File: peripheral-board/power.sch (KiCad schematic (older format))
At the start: 40 parts, among them CON4001 BARREL_JACK, Q4001 Q_PMOS_DGS, Q4002 Q_NMOS_DGS, U4001 AP1509, U4002 LM27313, U4003 LT3652

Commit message: power supply component placement
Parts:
- removed Q4001: Q_PMOS_DGS, symbol Q_PMOS_DGS
- removed Q4002: Q_NMOS_DGS, symbol Q_NMOS_DGS
- removed R4010, R4011: R, Resistors_SMD:R_0805, symbol R
- added Q4001: IRLML2244TRPbF, TO_SOT_Packages_SMD:SOT-23, symbol Q_PMOS_GSD
- C4007: value CP -> 100u
- C4010: value CP -> 220u
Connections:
- net labels added: SHDN_3, VAA, ~SHDN_24
- net labels removed: SHDN, VCC
- wire segments 82 -> 73
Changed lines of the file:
@@
 	1    0    0    -1
 $EndComp
-Text HLabel 950  3850 0    60   Input ~ 0
-SHDN
+Text HLabel 7300 5150 0    60   Input ~ 0
+SHDN_3
 $Comp
 L LT3652 U4003
@@
 BATTERY_NTC
 $Comp
-L PWR_FLAG #FLG4003
+L PWR_FLAG #FLG4004
 U 1 1 589AA4ED
 P 7500 2000
-F 0 "#FLG4003" H 7550 2050 50  0001 C CNN
+F 0 "#FLG4004" H 7550 2050 50  0001 C CNN
 F 1 "PWR_FLAG" H 7500 2174 50  0000 C CNN
 F 2 "" H -550 -1000 50  0001 C CNN
@@
 	0    -1   -1   0
 $EndComp
-$Comp
-L Q_PMOS_DGS Q4001
-U 1 1 589B3C76
-P 9750 1200
-F 0 "Q4001" V 10000 1200 50  0000 C CNN
-F 1 "Q_PMOS_DGS" V 10091 1200 50  0000 C CNN
-F 2 "" H 4850 -2550 50  0001 C CNN
-F 3 "" H 4650 -2650 50  0001 C CNN
-	1    9750 1200
-	0    -1   1    0
-$EndComp
 Connection ~ 10150 1300
 $Comp
@@
 	9950 1300 10950 1300
 $Comp
-L VCC #PWR4005
-U 1 1 589B6465
-P 10950 1300
-F 0 "#PWR4005" H 6250 -3050 50  0001 C CNN
-F 1 "VCC" H 10967 1473 50  0000 C CNN
-F 2 "" H 6250 -2900 50  0001 C CNN
-F 3 "" H 6250 -2900 50  0001 C CNN
-	1    10950 1300
-	1    0    0    -1
-$EndComp
-$Comp
 L PWR_FLAG #FLG4002
 U 1 1 589B64BF
@@
 P 9300 5400
 F 0 "C4010" H 9418 5446 50  0000 L CNN
-F 1 "CP" H 9418 5355 50  0000 L CNN
+F 1 "220u" H 9418 5355 50  0000 L CNN
 F 2 "" H 1088 -350 50  0001 C CNN
 F 3 "" H 1050 -200 50  0001 C CNN
@@
 P 7700 4600
 F 0 "C4007" V 7445 4600 50  0000 C CNN
-F 1 "CP" V 7536 4600 50  0000 C CNN
+F 1 "100u" V 7536 4600 50  0000 C CNN
 F 2 "" H 2438 -1550 50  0001 C CNN
 F 3 "" H 2400 -1400 50  0001 C CNN
@@
 Connection ~ 7900 4600
 $Comp
-L VCC #PWR4015
-U 1 1 589B80A7
-P 7900 4400
-F 0 "#PWR4015" H 7950 4450 50  0001 C CNN
-F 1 "VCC" H 7917 4573 50  0000 C CNN
-F 2 "" H 500 0   50  0001 C CNN
-F 3 "" H 500 0   50  0001 C CNN
-	1    7900 4400
-	1    0    0    -1
-$EndComp
-$Comp
-L GND #PWR4017
+L GND #PWR4016
 U 1 1 589B8109
 P 7550 4600
-F 0 "#PWR4017" H 7600 4650 50  0001 C CNN
+F 0 "#PWR4016" H 7600 4650 50  0001 C CNN
 F 1 "GND" V 7555 4472 50  0000 R CNN
 F 2 "" H 500 -200 50  0001 C CNN
@@
 Connection ~ 8600 5700
 $Comp
-L GND #PWR4021
+L GND #PWR4020
 U 1 1 589B85D2
 P 7750 5750
-F 0 "#PWR4021" H 7800 5800 50  0001 C CNN
+F 0 "#PWR4020" H 7800 5800 50  0001 C CNN
 F 1 "GND" H 7755 5577 50  0000 C CNN
 F 2 "" H 650 -750 50  0001 C CNN
@@
 Connection ~ 8600 5200
 $Comp
-L +3V3 #PWR4019
+L +3V3 #PWR4018
 U 1 1 589B91D5
 P 9900 5200
-F 0 "#PWR4019" H 9950 5250 50  0001 C CNN
+F 0 "#PWR4018" H 9950 5250 50  0001 C CNN
 F 1 "+3V3" H 9915 5373 50  0000 C CNN
 F 2 "" H 1700 -500 50  0001 C CNN
@@
 $EndComp
 $Comp
-L PWR_FLAG #FLG4005
+L PWR_FLAG #FLG4006
 U 1 1 589B9237
 P 9450 5200
-F 0 "#FLG4005" H 9500 5250 50  0001 C CNN
+F 0 "#FLG4006" H 9500 5250 50  0001 C CNN
 F 1 "PWR_FLAG" H 9450 5374 50  0000 C CNN
 F 2 "" H 1200 -550 50  0001 C CNN
 F 3 "" H 1200 -550 50  0001 C CNN
 	1    9450 5200
-	1    0    0    -1
-$EndComp
-$Comp
-L VCC #PWR4014
-U 1 1 589BA1AA
-P 3000 4400
-F 0 "#PWR4014" H 3050 4450 50  0001 C CNN
-F 1 "VCC" H 3017 4573 50  0000 C CNN
-F 2 "" H -4400 0   50  0001 C CNN
-F 3 "" H -4400 0   50  0001 C CNN
-	1    3000 4400
 	1    0    0    -1
 $EndComp
@@
 	3000 4400 3000 4500
 $Comp
-L GND #PWR4016
+L GND #PWR4015
 U 1 1 589BA9B7
 P 2650 4450
-F 0 "#PWR4016" H 2700 4500 50  0001 C CNN
+F 0 "#PWR4015" H 2700 4500 50  0001 C CNN
 F 1 "GND" V 2655 4322 50  0000 R CNN
 F 2 "" H -4450 -2050 50  0001 C CNN
@@
 $EndComp
 $Comp
-L GND #PWR4020
+L GND #PWR4019
 U 1 1 589BAA61
 P 3000 5750
-F 0 "#PWR4020" H 3050 5800 50  0001 C CNN
+F 0 "#PWR4019" H 3050 5800 50  0001 C CNN
 F 1 "GND" H 3005 5577 50  0000 C CNN
 F 2 "" H -4100 -750 50  0001 C CNN
@@
 U 1 1 589BAB6A
 P 3950 5100
-F 0 "R4012" V 3850 4950 50  0000 C CNN
+F 0 "R4012" V 3850 5150 50  0000 C CNN
 F 1 "270k" V 3950 5100 50  0000 C CNN
 F 2 "Resistors_SMD:R_0805" V -1070 -400 50  0001 C CNN
@@
 U 1 1 589BAE7E
 P 3750 5550
-F 0 "R4013" H 3820 5596 50  0000 L CNN
-F 1 "13.3k" H 3820 5505 50  0000 L CNN
+F 0 "R4013" H 3450 5550 50  0000 L CNN
+F 1 "13.3k" H 3500 5450 50  0000 L CNN
 F 2 "Resistors_SMD:R_0805" V -1420 -200 50  0001 C CNN
 F 3 "" H -1350 -200 50  0001 C CNN
@@
 	3750 5100 3750 5400
 Connection ~ 3750 5100
-Wire Wire Line
-	2100 5700 4400 5700
 Connection ~ 3000 5700
 Wire Wire Line
@@
 U 1 1 589BB298
 P 3950 5300
-F 0 "C4008" V 4050 5400 50  0000 C CNN
-F 1 "120p" V 4050 5200 50  0000 C CNN
+F 0 "C4008" V 4100 5300 50  0000 C CNN
+F 1 "120p" V 4000 5450 50  0000 C CNN
 F 2 "Capacitors_SMD:C_0805" H -912 -350 50  0001 C CNN
 F 3 "" H -950 -200 50  0001 C CNN
@@
 Connection ~ 3750 5300
 $Comp
-L +24V #PWR4018
+L +24V #PWR4017
 U 1 1 589BBC33
 P 4800 5000
-F 0 "#PWR4018" H 4850 5050 50  0001 C CNN
+F 0 "#PWR4017" H 4850 5050 50  0001 C CNN
 F 1 "+24V" H 4815 5173 50  0000 C CNN
 F 2 "" H -100 -50 50  0001 C CNN
@@
 $EndComp
 $Comp
-L PWR_FLAG #FLG4004
+L PWR_FLAG #FLG4005
 U 1 1 589BBD5B
 P 4500 5000
-F 0 "#FLG4004" H 4550 5050 50  0001 C CNN
+F 0 "#FLG4005" H 4550 5050 50  0001 C CNN
 F 1 "PWR_FLAG" H 4500 5174 50  0000 C CNN
 F 2 "" H -400 -550 50  0001 C CNN
@@
 	4500 5000 4500 5100
 Connection ~ 4500 5100
-$Comp
-L Q_NMOS_DGS Q4002
-U 1 1 589BE67A
-P 2000 5500
-F 0 "Q4002" H 2205 5546 50  0000 L CNN
-F 1 "Q_NMOS_DGS" H 2205 5455 50  0000 L CNN
-F 2 "" H 700 550 50  0001 C CNN
-F 3 "" H 500 450 50  0001 C CNN
-	1    2000 5500
-	1    0    0    -1
-$EndComp
-Wire Wire Line
-	7300 5150 6600 5150
-Wire Wire Line
-	6600 5150 6600 3850
-Wire Wire Line
-	6600 3850 950  3850
-Wire Wire Line
-	2100 5000 2100 5300
-Wire Wire Line
-	2100 5050 2300 5050
-$Comp
-L R R4011
-U 1 1 589BF24E
-P 2100 4850
-F 0 "R4011" H 2170 4896 50  0000 L CNN
-F 1 "R" H 2170 4805 50  0000 L CNN
-F 2 "Resistors_SMD:R_0805" V -120 -50 50  0001 C CNN
-F 3 "" H -50 -50 50  0001 C CNN
-	1    2100 4850
-	1    0    0    -1
-$EndComp
-Connection ~ 2100 5050
-Wire Wire Line
-	1800 5500 1500 5500
-Wire Wire Line
-	1500 5500 1500 3850
-Connection ~ 1500 3850
-$Comp
-L R R4010
-U 1 1 589BF943
-P 1150 4050
-F 0 "R4010" H 1220 4096 50  0000 L CNN
-F 1 "R" H 1220 4005 50  0000 L CNN
-F 2 "Resistors_SMD:R_0805" V 30  -250 50  0001 C CNN
-F 3 "" H 100 -250 50  0001 C CNN
-	1    1150 4050
-	1    0    0    -1
-$EndComp
-$Comp
-L GND #PWR4013
-U 1 1 589BF9D9
-P 1150 4250
-F 0 "#PWR4013" H 200 -500 50  0001 C CNN
-F 1 "GND" H 1155 4077 50  0000 C CNN
-F 2 "" H 200 -250 50  0001 C CNN
-F 3 "" H 200 -250 50  0001 C CNN
-	1    1150 4250
-	1    0    0    -1
-$EndComp
-Wire Wire Line
-	1150 4250 1150 4200
-Wire Wire Line
-	1150 3900 1150 3850
-Connection ~ 1150 3850
+Text HLabel 2300 5050 0    60   Input ~ 0
+~SHDN_24
+Wire Wire Line
+	4400 5700 3000 5700
+$Comp
+L VAA #PWR4005
+U 1 1 58A8EB71
+P 10950 1300
+F 0 "#PWR4005" H 11000 1350 50  0001 C CNN
+F 1 "VAA" H 10967 1473 50  0000 C CNN
+F 2 "" H 100 550 50  0001 C CNN
+F 3 "" H 100 550 50  0001 C CNN
+	1    10950 1300
+	1    0    0    -1
+$EndComp
+$Comp
+L VAA #PWR4014
+U 1 1 58A8ECBE
+P 7900 4400
+F 0 "#PWR4014" H 7950 4450 50  0001 C CNN
+F 1 "VAA" H 7917 4573 50  0000 C CNN
+F 2 "" H -2950 3650 50  0001 C CNN
+F 3 "" H -2950 3650 50  0001 C CNN
+	1    7900 4400
+	1    0    0    -1
+$EndComp
+$Comp
+L VAA #PWR4013
+U 1 1 58A8F0E4
+P 3000 4400
+F 0 "#PWR4013" H 3050 4450 50  0001 C CNN
+F 1 "VAA" H 3017 4573 50  0000 C CNN
+F 2 "" H -7850 3650 50  0001 C CNN
+F 3 "" H -7850 3650 50  0001 C CNN
+	1    3000 4400
+	1    0    0    -1
+$EndComp
+$Comp
+L PWR_FLAG #FLG4003
+U 1 1 58A910EB
+P 2200 1400
+F 0 "#FLG4003" H -550 175 50  0001 C CNN
+F 1 "PWR_FLAG" H 2200 1574 50  0000 C CNN
+F 2 "" H -550 100 50  0001 C CNN
+F 3 "" H -550 100 50  0001 C CNN
+	1    2200 1400
+	0    1    1    0
+$EndComp
+$Comp
+L Q_PMOS_GSD Q4001
+U 1 1 58A96BE8
+P 9750 1200
+F 0 "Q4001" V 10000 1200 50  0000 C CNN
+F 1 "IRLML2244TRPbF" V 10091 1200 50  0000 C CNN
+F 2 "TO_SOT_Packages_SMD:SOT-23" H -450 -500 50  0001 C CNN
+F 3 "" H -650 -600 50  0001 C CNN
+	1    9750 1200
+	0    -1   1    0
+$EndComp
 $EndSCHEMATC

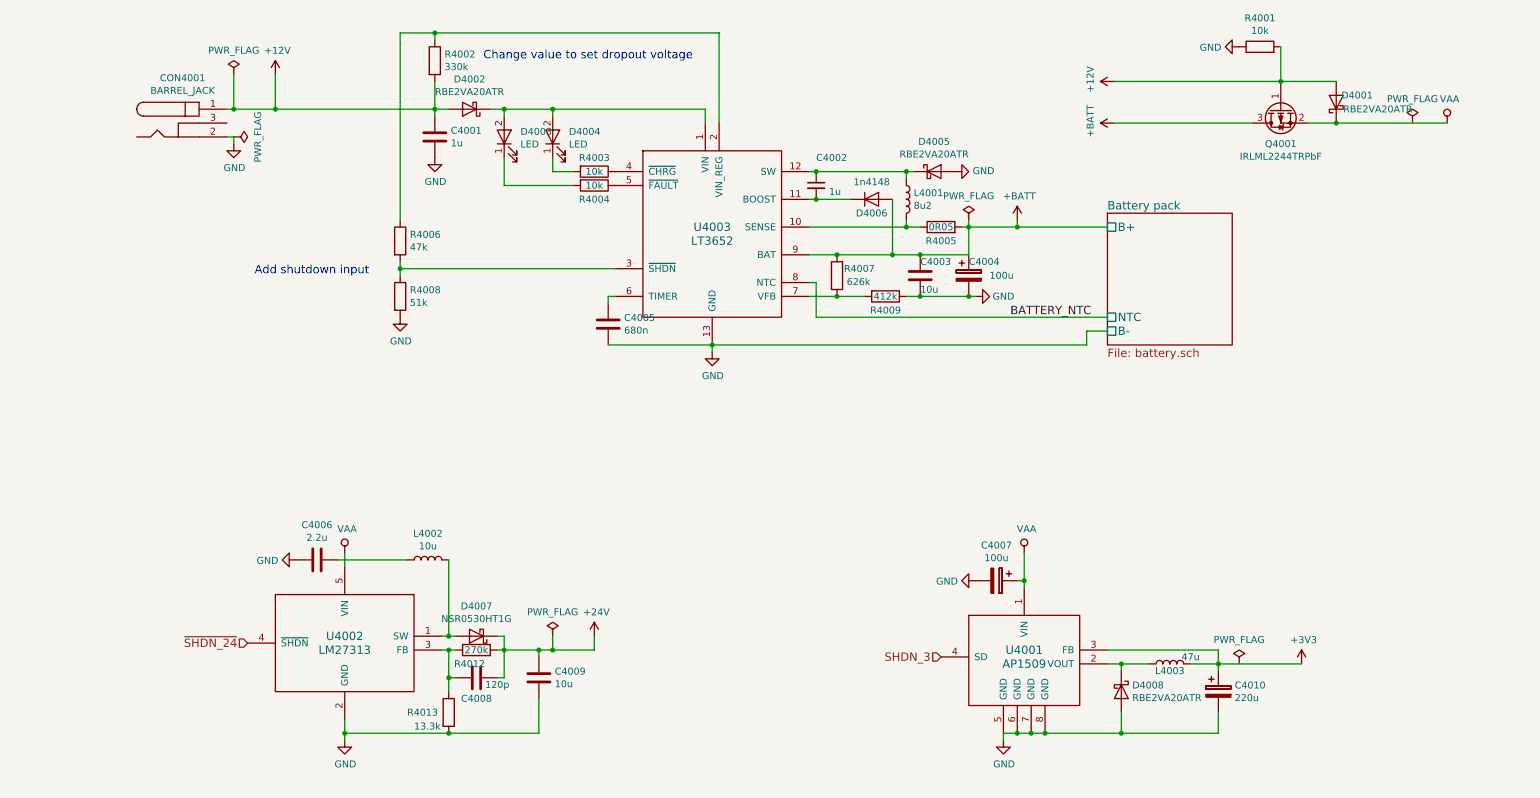
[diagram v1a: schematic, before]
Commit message: audio components placement
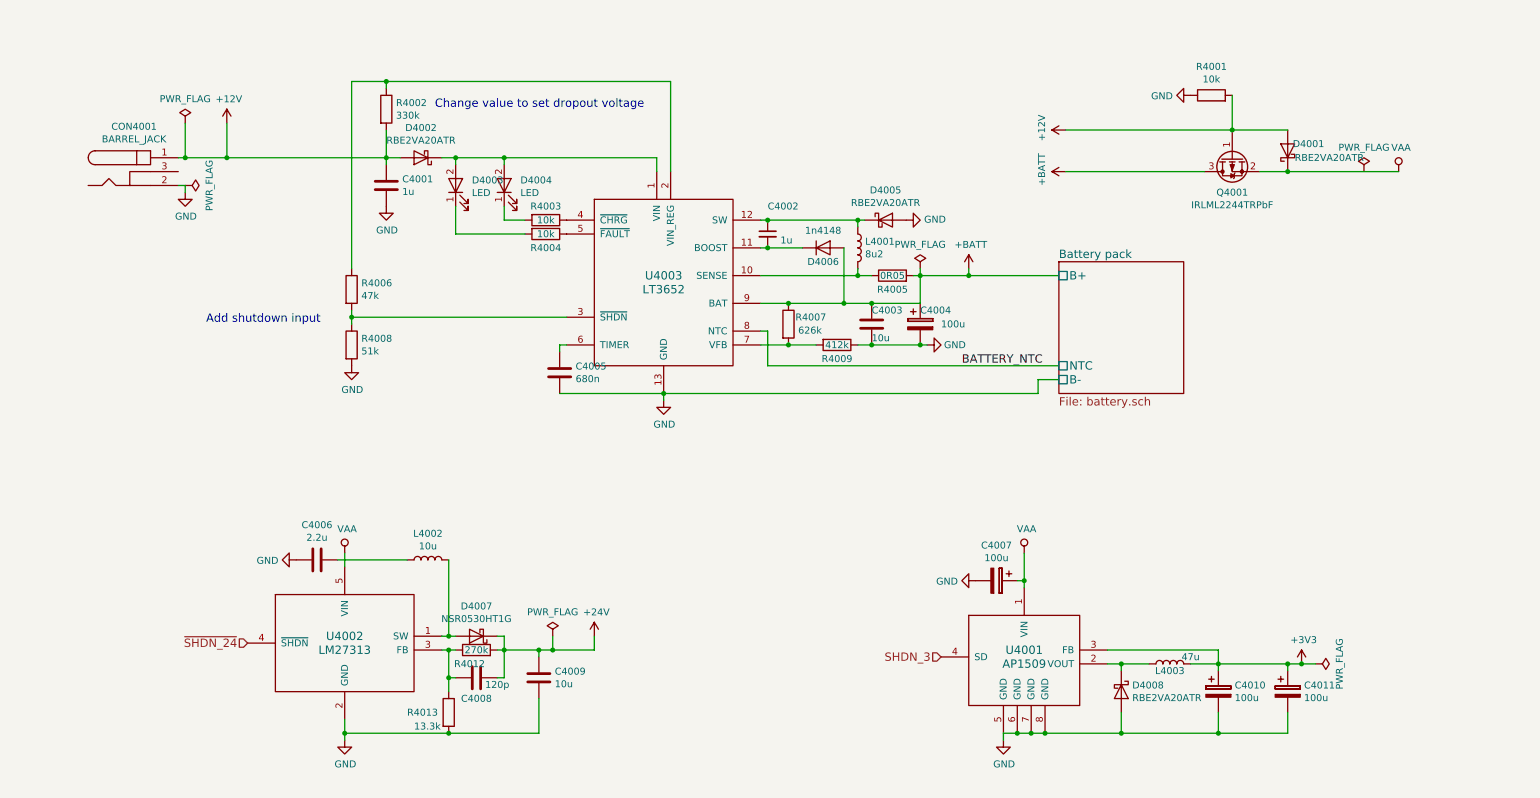
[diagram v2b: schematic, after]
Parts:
- added C4011: 100u, Capacitors_SMD:c_elec_6.3x5.8, symbol CP
- C4010: value 220u -> 100u; footprint (none) -> Capacitors_SMD:c_elec_6.3x5.8
- L4003: footprint Choke_SMD:Choke_SMD_7.3x7.3_H4.5 -> Choke_SMD:Choke_SMD_12x12mm_h6mm
- R4005: footprint Resistors_SMD:R_0805 -> Resistors_SMD:R_1812
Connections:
- net +3V3: now also C4011.1
- net GND: now also C4011.2
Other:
- moved on the sheet: C4001, C4002, C4003, C4004, C4005, CON4001, D4001, D4002, D4003, D4004, D4005, D4006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

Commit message: routed spi
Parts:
- removed D4003, D4004: LED, symbol LED
- added D4003: SSL-LX3059IGW-CA, LEDs:LED-5MM-3, symbol LED_Dual_CAC
- C4004, C4007: footprint (none) -> Capacitors_Tantalum_SMD:TantalC_SizeD_EIA-7343_Reflow
- L4001, L4002: footprint Choke_SMD:Choke_SMD_1206_Standard -> Choke_SMD:Choke_SMD_6.3x6.3_H3
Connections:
- net VAA: now also C4006.1, L4002.1
- net at D4002.1 (K), U4003.1 (VIN): now also D4003.2 (A)
- net at R4003.2: now also D4003.1 (K1)
- net at R4004.2: now also D4003.3 (K2)

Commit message: routed audio circuitry
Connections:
- net CHRG_SENSE: now reaches L4001.2, R4005.1, U4003.10 (SENSE)
- net CHRG_SW: now reaches C4002.1, D4005.1 (K), L4001.1, U4003.12 (SW)
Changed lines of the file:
@@
 	2950 4450 3450 4450
 Connection ~ 3000 4450
+Text Label 6000 2000 0    60   ~ 0
+CHRG_SW
+Text Label 6000 2400 0    60   ~ 0
+CHRG_SENSE
 $EndSCHEMATC
